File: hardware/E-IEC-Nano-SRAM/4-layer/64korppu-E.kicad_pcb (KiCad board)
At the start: 4 copper layers, 70 x 60 mm, 27 parts, among them J1 DIN-6_IEC, J2 Floppy_34pin, J3 DC_Jack, U1 Arduino_Nano, U2 23LC1024, U3 74HC595

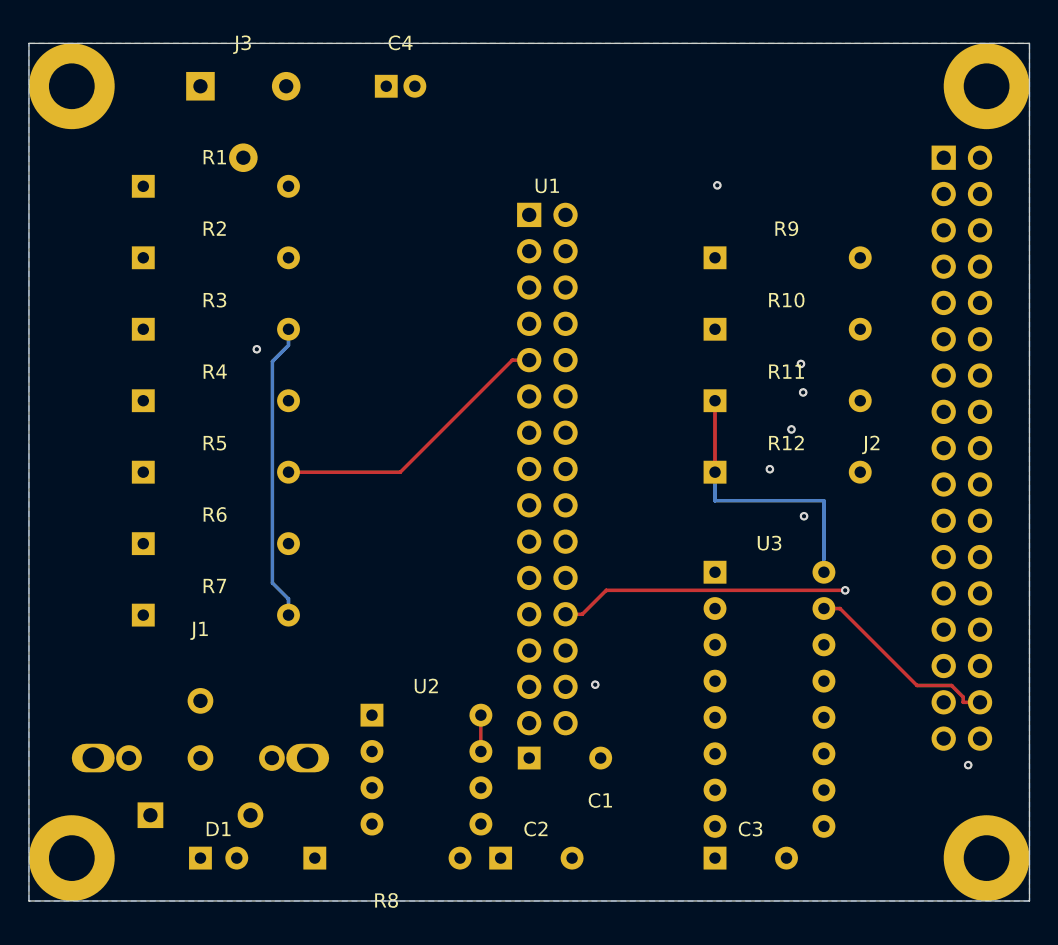
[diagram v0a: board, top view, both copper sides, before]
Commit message: Fix 4-layer PCB: redesign layout to eliminate all body collisions, 0/0/0 DRC
Repositioned all 27 components to fix 15 body collisions with 1mm clearance.
Added manual +5V trace on B.Cu for U3.16→R12.1. Freerouting autorouted
remaining nets. DRC: 0 critical, 0 warnings, 0 unconnected.

Co-Authored-By: Claude Opus 4.6 <noreply@anthropic.com>
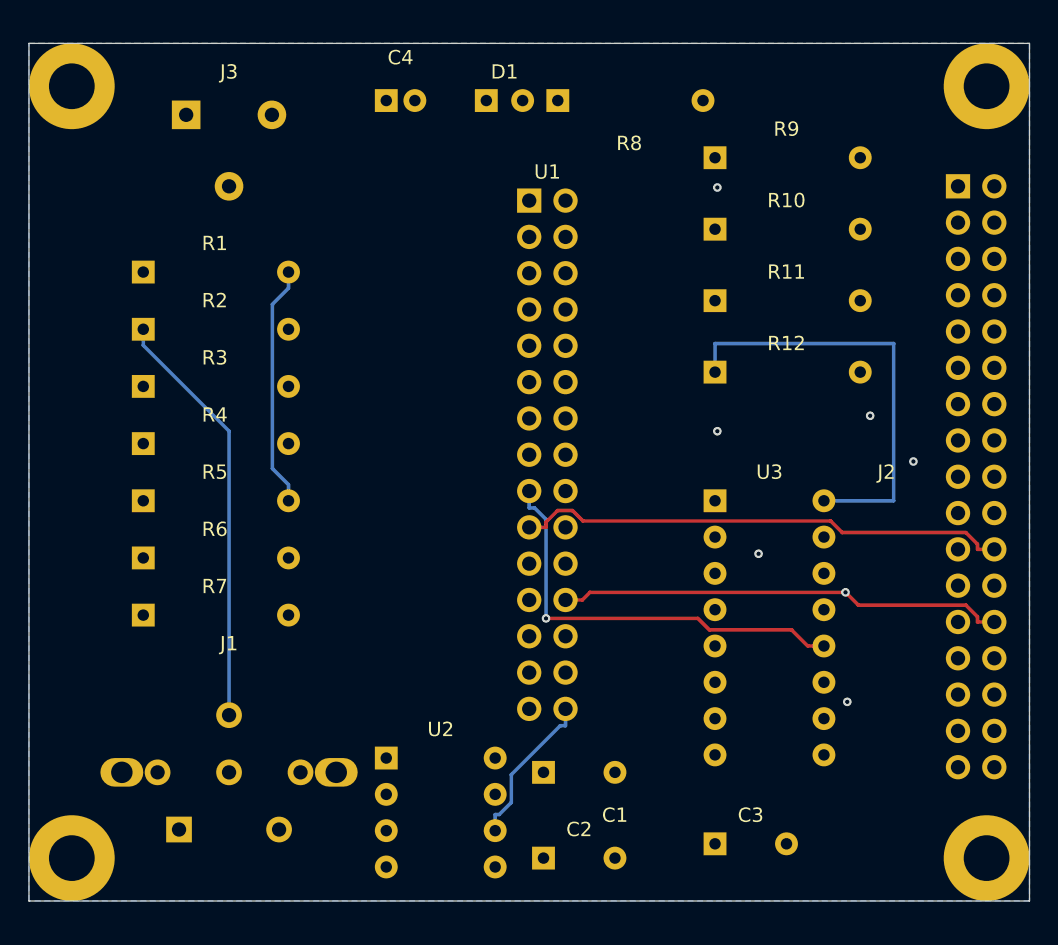
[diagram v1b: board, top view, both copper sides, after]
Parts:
- moved D1 56.6 mm to (132.0, 104.0)
- moved R8 55.7 mm to (137.0, 104.0)
- moved R10 7.00 mm to (148.0, 113.0)
- moved R11 7.00 mm to (148.0, 118.0)
- moved R12 7.00 mm to (148.0, 123.0)
- moved R9 7.00 mm to (148.0, 108.0)
- moved R1 6.00 mm to (108.0, 116.0)
- moved R2 5.00 mm to (108.0, 120.0)
- moved U3 5.00 mm to (148.0, 132.0)
- moved R3 4.00 mm to (108.0, 124.0)
- moved U2 3.16 mm to (125.0, 150.0)
- moved C2 3.00 mm to (136.0, 157.0)
- moved R4 3.00 mm to (108.0, 128.0)
- moved J1 2.24 mm to (114.0, 151.0)
- moved J2 2.24 mm to (165.0, 110.0)
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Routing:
- net LED_ANODE: track 38.7 -> 23.2 mm
- net FLOPPY_WGATE: track 36.1 -> 23.6 mm, vias 1 -> 0
- net NANO_D4: track 46.8 -> 34.7 mm
- net FLOPPY_SIDE1: track 13.9 -> 25.1 mm, vias 0 -> 1
- net FLOPPY_DIR: track 35.7 -> 24.7 mm, vias 1 -> 0
- net FLOPPY_MOTOR: track 34.9 -> 25.3 mm
- net +5V: track 22.2 -> 30.4 mm
- net FLOPPY_STEP: track 32.8 -> 24.7 mm, vias 1 -> 0
- net FLOPPY_TRK00: track 54.6 -> 62.2 mm
- net NANO_D3: track 42.5 -> 35.3 mm, vias 1 -> 0
- net SPI_MOSI: track 33.4 -> 38.7 mm
- net NANO_D2: track 41.0 -> 35.9 mm
- net FLOPPY_DENSITY: track 48.7 -> 43.7 mm
- net FLOPPY_MOTEA: track 34.5 -> 29.7 mm, vias 1 -> 0
- net IEC_ATN: track 40.5 -> 36.3 mm
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
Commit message: Add 14 diagnostic test points to 4-layer PCB, 0/0/0 DRC
Added SMD test points on B.Cu (back side) along left edge at x=103:
GND, +5V, IEC_ATN/CLK/DATA, FLOPPY_MOTOR/STEP/RDATA/WDATA/SIDE1,
SPI_SCK/MOSI/MISO/CS_SRAM.

Manual +5V trace on B.Cu connecting U3.16 to R12.1 (routed around
right side of U3 at x=160.5). Updated pcb-validate.py with TestPoint
body dimensions.

DRC: 0 critical, 0 warnings, 0 unconnected.

Co-Authored-By: Claude Opus 4.6 <noreply@anthropic.com>
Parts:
- added TP1: GND, TestPoint:TestPoint_Pad_D1.5_SMD, B.Cu at (103.0, 108.0)
- added TP10: FLOPPY_SIDE1, TestPoint:TestPoint_Pad_D1.5_SMD, B.Cu at (103.0, 130.5)
- added TP11: SPI_SCK, TestPoint:TestPoint_Pad_D1.5_SMD, B.Cu at (103.0, 133.0)
- added TP12: SPI_MOSI, TestPoint:TestPoint_Pad_D1.5_SMD, B.Cu at (103.0, 135.5)
- added TP13: SPI_MISO, TestPoint:TestPoint_Pad_D1.5_SMD, B.Cu at (103.0, 138.0)
- added TP14: SPI_CS_SRAM, TestPoint:TestPoint_Pad_D1.5_SMD, B.Cu at (103.0, 140.5)
- added TP2: +5V, TestPoint:TestPoint_Pad_D1.5_SMD, B.Cu at (103.0, 110.5)
- added TP3: IEC_ATN, TestPoint:TestPoint_Pad_D1.5_SMD, B.Cu at (103.0, 113.0)
- added TP4: IEC_CLK, TestPoint:TestPoint_Pad_D1.5_SMD, B.Cu at (103.0, 115.5)
- added TP5: IEC_DATA, TestPoint:TestPoint_Pad_D1.5_SMD, B.Cu at (103.0, 118.0)
- added TP6: FLOPPY_MOTOR, TestPoint:TestPoint_Pad_D1.5_SMD, B.Cu at (103.0, 120.5)
- added TP7: FLOPPY_STEP, TestPoint:TestPoint_Pad_D1.5_SMD, B.Cu at (103.0, 123.0)
- added TP8: FLOPPY_RDATA, TestPoint:TestPoint_Pad_D1.5_SMD, B.Cu at (103.0, 125.5)
- added TP9: FLOPPY_WDATA, TestPoint:TestPoint_Pad_D1.5_SMD, B.Cu at (103.0, 128.0)
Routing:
- net FLOPPY_STEP: track 24.7 -> 88.2 mm, vias 0 -> 2
- net FLOPPY_MOTOR: track 25.3 -> 83.8 mm, vias 1 -> 2
- net FLOPPY_RDATA: track 61.0 -> 116.8 mm, vias 1 -> 2
- net FLOPPY_SIDE1: track 25.1 -> 78.4 mm, vias 1 -> 3
- net SPI_SCK: track 29.8 -> 81.1 mm, vias 0 -> 1
- net SPI_MOSI: track 38.7 -> 79.4 mm, vias 0 -> 1
- net SPI_MISO: track 12.5 -> 48.8 mm, vias 0 -> 1
- net FLOPPY_WDATA: track 34.6 -> 69.3 mm, vias 0 -> 1
- net SPI_CS_SRAM: track 14.0 -> 46.1 mm, vias 0 -> 1
- net IEC_DATA: track 31.6 -> 39.7 mm
- net IEC_CLK: track 29.5 -> 36.7 mm
- net FLOPPY_TRK00: track 62.2 -> 68.8 mm
- net FLOPPY_DRVSEL: track 32.4 -> 25.9 mm, vias 1 -> 0
- net IEC_ATN: track 36.3 -> 42.6 mm
- net FLOPPY_DENSITY: track 43.7 -> 41.3 mm
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
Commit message: Switch SRAM from 23LC1024 (128KB) to 23LC256 (32KB), fix 74HC595 QA pin docs
- Replace 23LC1024 with 23LC256: same DIP-8 pinout, 16-bit addressing
- SRAM driver: 24-bit → 16-bit address (drop one spi_transfer call)
- SimAVR harness: update SRAM emulation to 2-byte addressing and 32KB
- Fix piirikaavio.md: QA was incorrectly marked as unused (is /SIDE1)
- Fix shiftreg.h bit mapping comment to match actual hardware wiring
- Update all docs, schematics, PCB files, tools for both 2-layer and 4-layer

Actual SRAM usage is ~22KB, so 32KB is sufficient with margin.

Co-Authored-By: Claude Opus 4.6 <noreply@anthropic.com>
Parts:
- U2: value 23LC1024 -> 23LC256
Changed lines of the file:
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@@
 			)
 		)
-		(property "Value" "23LC1024"
+		(property "Value" "23LC256"
 			(at 140 195 0)
 			(layer "F.Fab")

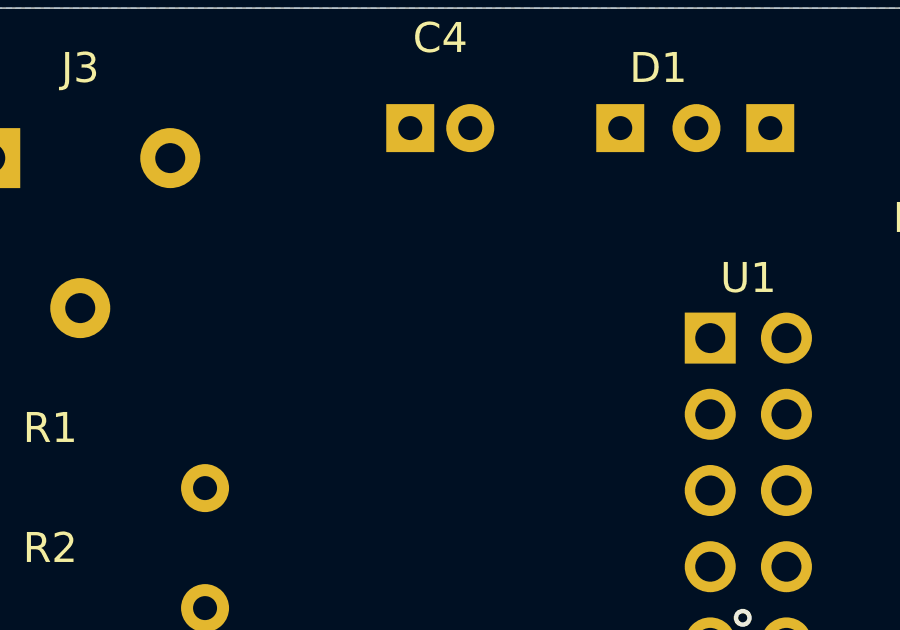
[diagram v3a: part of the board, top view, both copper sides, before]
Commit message: Add "karski by design 2026 rev 001" board label to both PCBs
Add copper layer text label on F.Cu for 2-layer and 4-layer PCBs.
Resize script recreates the label automatically on each resize.
Fix SetIsBold→SetBold for KiCad 9 Python API.

Co-Authored-By: Claude Opus 4.6 <noreply@anthropic.com>
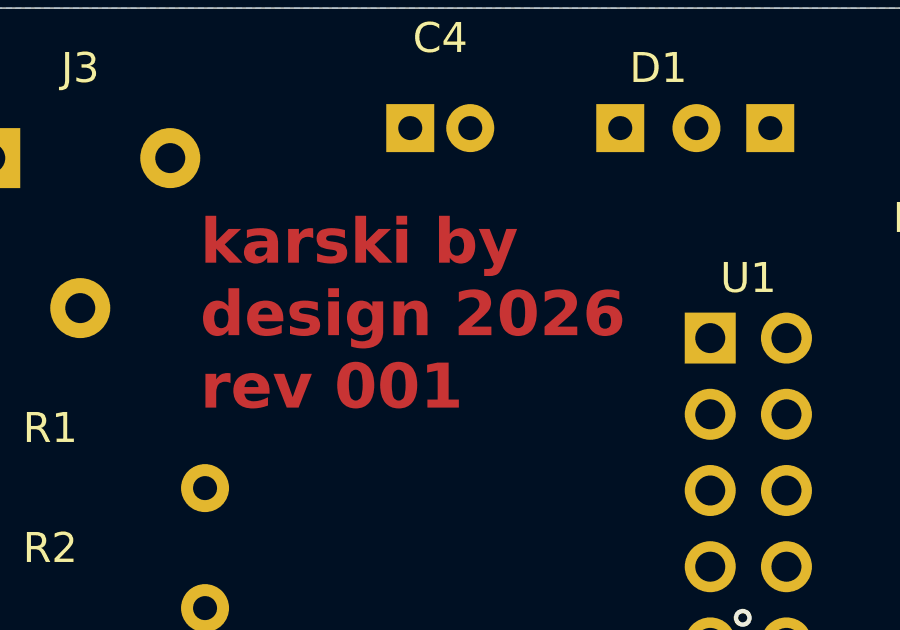
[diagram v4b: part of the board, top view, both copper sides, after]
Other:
- board text added: "karski by design 2026 rev 001"
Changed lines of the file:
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@@
 		(layer "Edge.Cuts")
+	)
+	(gr_text "karski by\ndesign 2026\nrev 001"
+		(at 118 113.5 0)
+		(layer "F.Cu")
+		(effects
+			(font
+				(size 1.5 1.5)
+				(thickness 0.3)
+				(bold yes)
+			)
+			(justify left bottom)
+		)
 	)
 	(via
